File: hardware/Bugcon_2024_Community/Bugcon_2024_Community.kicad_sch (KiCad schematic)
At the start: 37 parts, among them J2 Add_On, J3 OLED, J4 Battery, J5 Battery, P1 USB_C_Plug_USB2.0, Q1 DMG3415U-7, SW1 ON, U1 ESP32-C6-WROOM-1U-N4, U2 AP2112K-3.3

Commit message: feat(Hw): Update community PCB
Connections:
- net LED1: now also U1.27 (IO2)
- net LED2: now also U1.26 (IO3)
- net GPIO2: no longer names the net of J2.6 (Pin_6)
- net GPIO2: no longer U1.27 (IO2)
- net GPIO3: no longer names the net of J2.5 (Pin_5)
- net GPIO3: no longer U1.26 (IO3)
- no-connect marks 7 -> 9

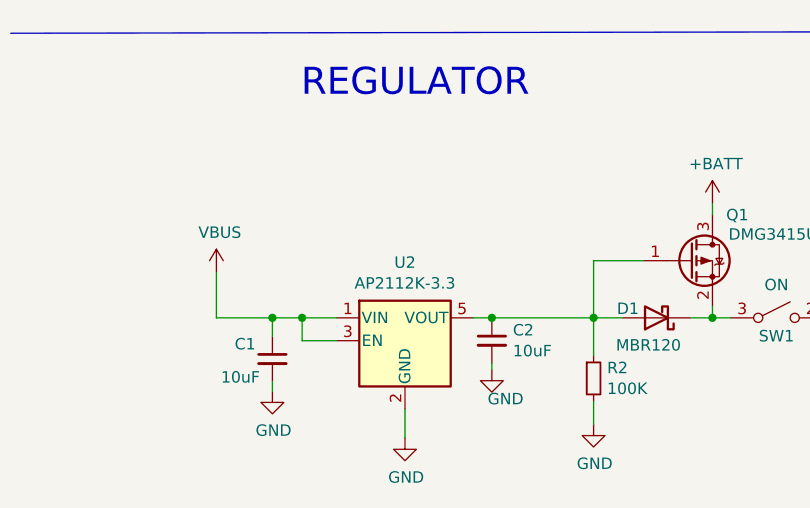
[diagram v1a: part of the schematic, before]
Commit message: feat(Hw):Added_1A_Regulator
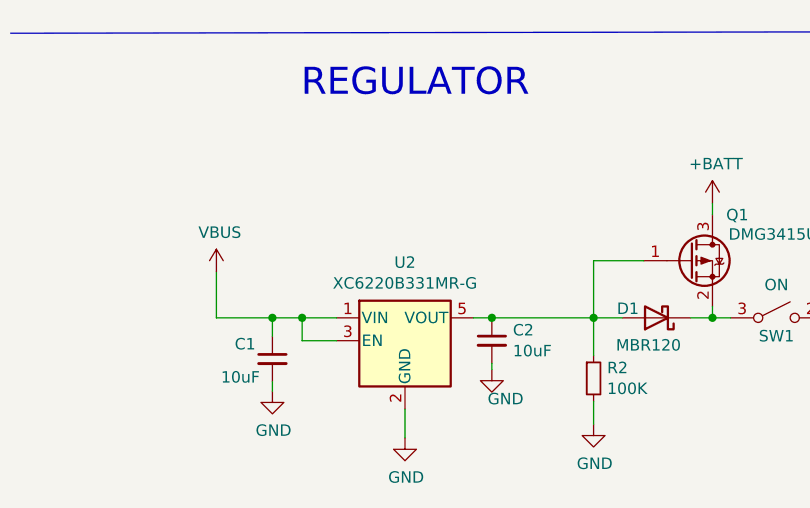
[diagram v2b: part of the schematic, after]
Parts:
- J3: manf# Display OLED 128Ã—32 0.91 I2C SSD1306 Blanco / Azul -> Display OLED 128x32 0.91 I2C SSD1306 Blanco / Azul
- U2: value AP2112K-3.3 -> XC6220B331MR-G; LCSC# C51118 -> C86534; manf# AP2112K3.3TRG -> XC6220B331MR-G
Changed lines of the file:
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@@
 			)
 		)
-		(property "manf#" "Display OLED 128Ã—32 0.91 I2C SSD1306 Blanco / Azul"
+		(property "manf#" "Display OLED 128x32 0.91 I2C SSD1306 Blanco / Azul"
 			(at 115.57 123.19 0)
 			(effects
@@
 			)
 		)
-		(property "Value" "AP2112K-3.3"
+		(property "Value" "XC6220B331MR-G"
 			(at 56.261 171.8056 0)
 			(effects
@@
 			)
 		)
-		(property "manf#" "AP2112K3.3TRG"
+		(property "manf#" "XC6220B331MR-G "
 			(at 56.261 178.181 0)
 			(effects
@@
 			)
 		)
-		(property "LCSC#" "C51118"
+		(property "LCSC#" "C86534"
 			(at 56.261 178.181 0)
 			(effects

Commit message: feat(Hw): Update ground areas
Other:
- company: (none) -> Electronic Cats
- title: (none) -> Bugcon_2024_Community
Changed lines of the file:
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@@
 	(generator_version "8.0")
 	(paper "A4")
+	(title_block
+		(title "Bugcon_2024_Community")
+		(date "2024-09-05")
+		(rev "v1.0")
+		(company "Electronic Cats")
+		(comment 1 "Lizeth Gallegos Martínez")
+	)
 	(junction
 		(at 185.674 69.088)

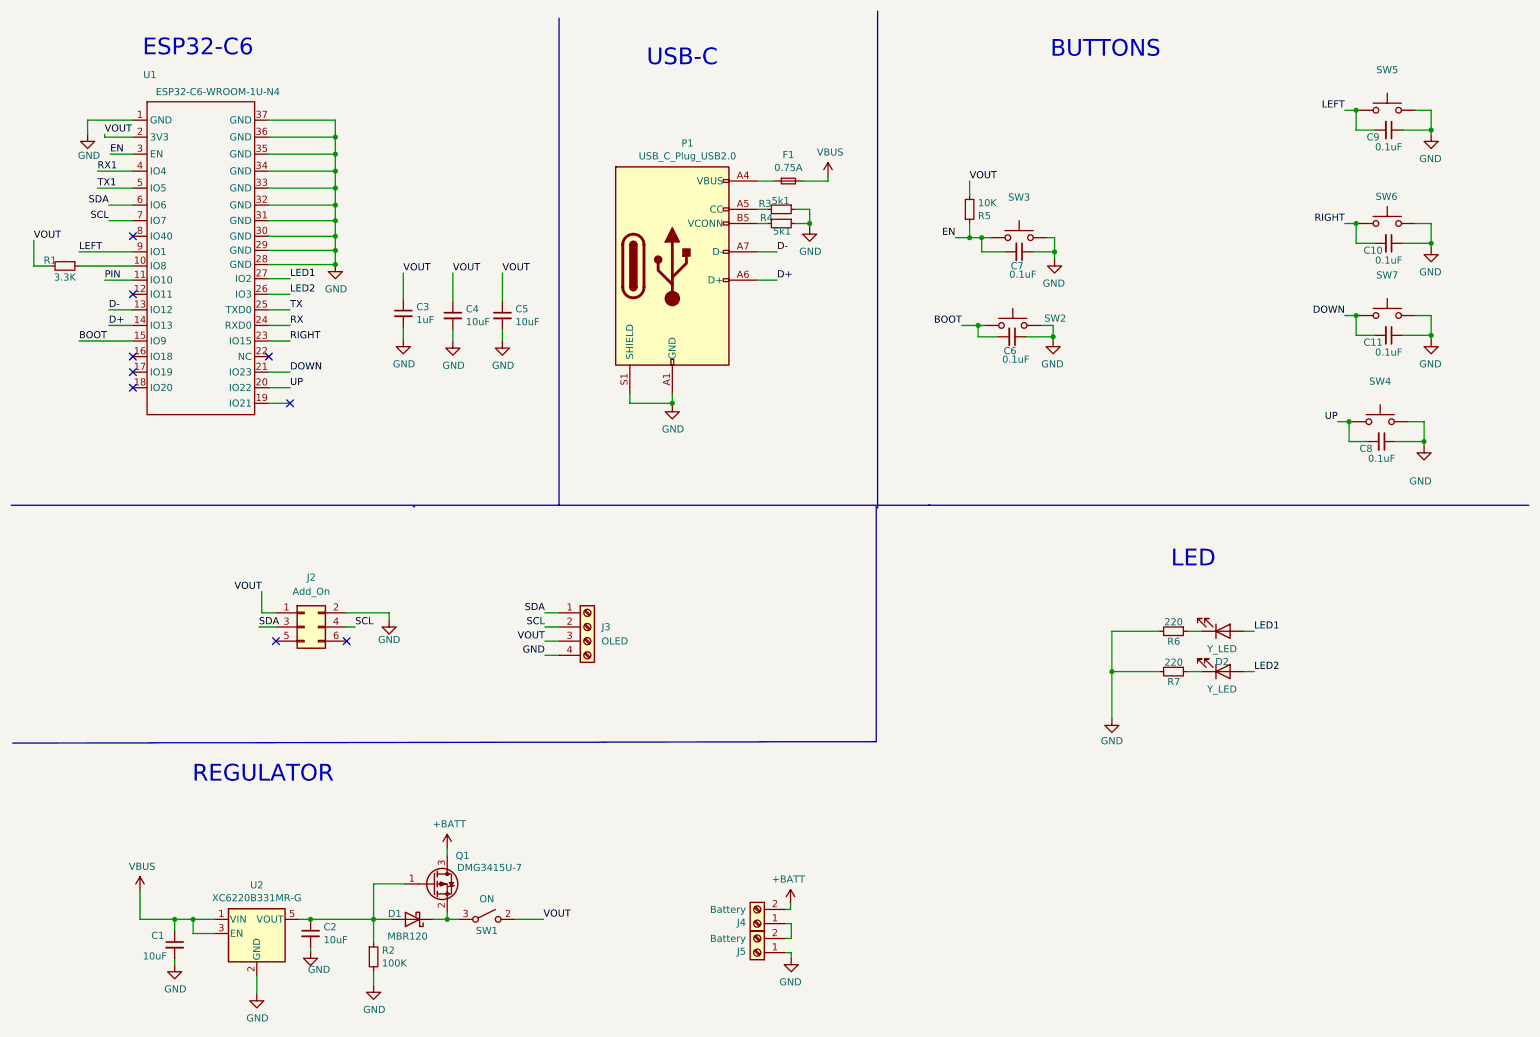
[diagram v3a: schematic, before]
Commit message: feat(Hw): Change LEDs
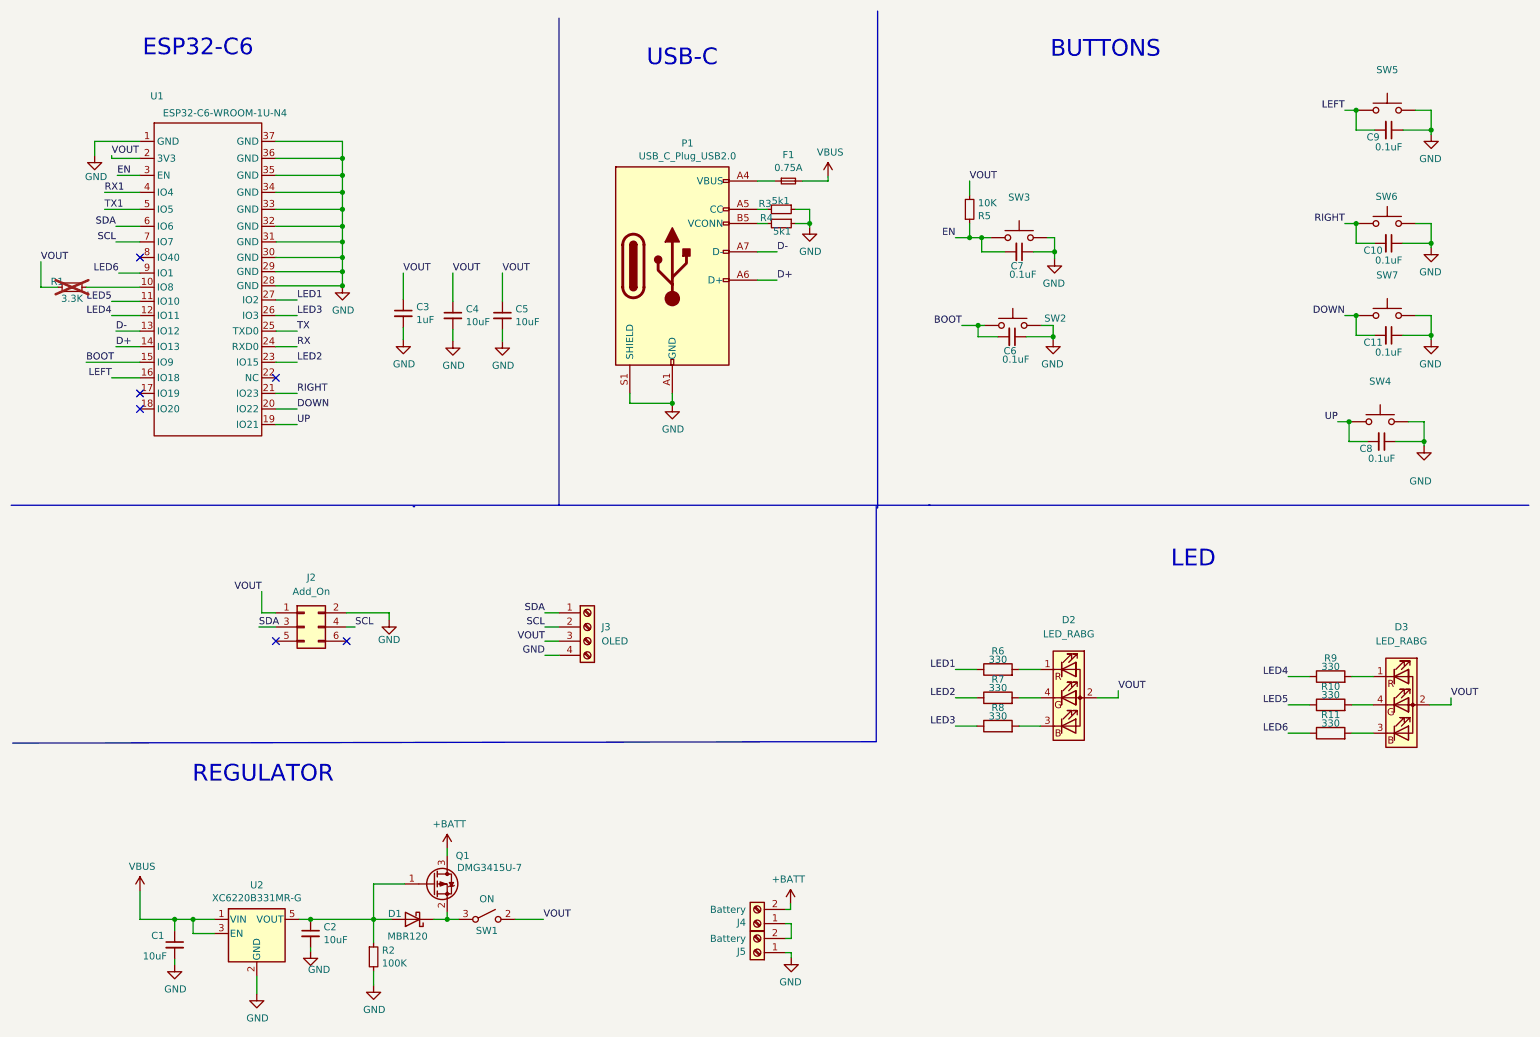
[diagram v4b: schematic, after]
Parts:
- removed D2, D3: Y_LED, Library:LYT77K-K2M1, symbol Device:LED
- removed R6, R7: 220, Resistor_SMD:R_0603_1608Metric_Pad0.98x0.95mm_HandSolder, symbol Device:R_Small
- added D2, D3: LED_RABG, Library:AAA3528SURKCGKC09, symbol Device:LED_RABG
- added R10, R11, R6, R7, R8, R9: 330, Resistor_SMD:R_0603_1608Metric, symbol Device:R
- R1: now not fitted
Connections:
- net DOWN: now also U1.20 (IO22); no longer U1.21 (IO23)
- net LED1: now also R6.1
- net LED2: now also U1.23 (IO15), R7.1; no longer U1.26 (IO3)
- net LEFT: now also U1.16 (IO18); no longer U1.9 (IO1)
- net RIGHT: now also U1.21 (IO23); no longer U1.23 (IO15)
- net UP: now also U1.19 (IO21); no longer U1.20 (IO22)
- net VOUT: now also D2.2 (A), D3.2 (A)
- net LED4: now reaches U1.12 (IO11)
- net LED4: now also R9.1
- net PIN renamed LED5
- net LED5: now also R10.1
- new net: D3.3 (BK), R11.2
- new net: D2.4 (GK), R7.2
- new net: D3.1 (RK), R9.2
- new net: D3.4 (GK), R10.2
- new net: D2.1 (RK), R6.2
- new net: D2.3 (BK), R8.2
- new net LED3: R8.1, U1.26 (IO3)
- new net LED6: R11.1, U1.9 (IO1)
- no-connect marks 9 -> 6
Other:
- moved on the sheet: U1
